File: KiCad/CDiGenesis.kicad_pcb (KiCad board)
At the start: 2 copper layers, 32 x 28 mm, 7 parts, among them J1 Genesis, J2 CDi, J3 Conn_01x03, U1 ATtiny1616-M

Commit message: Add silkscreen, nearing code completion
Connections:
- net /BTN_A/B renamed /BTN_B/A
- net /BTN_S/C renamed /BTN_C/S
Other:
- board text added: "+5V"
- board text added: "GND"
- board text added: "RTS"
- board text added: "RXD"
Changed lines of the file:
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@@
 	(net 2 "+5V")
 	(net 3 "/D_Up")
-	(net 4 "/BTN_A{slash}B")
-	(net 5 "/BTN_S{slash}C")
+	(net 4 "/BTN_B{slash}A")
+	(net 5 "/BTN_C{slash}S")
 	(net 6 "/D_Left")
 	(net 7 "/Select")
@@
 			(size 0.143431 0.143431)
 			(layers "F.Cu" "F.Mask" "F.Paste")
-			(net 4 "/BTN_A{slash}B")
+			(net 4 "/BTN_B{slash}A")
 			(pinfunction "PA2")
 			(pintype "bidirectional")
@@
 			(layers "F.Cu" "F.Mask" "F.Paste")
 			(roundrect_rratio 0.25)
-			(net 5 "/BTN_S{slash}C")
+			(net 5 "/BTN_C{slash}S")
 			(pinfunction "PA7")
 			(pintype "bidirectional")
@@
 			(layers "*.Cu" "*.Mask")
 			(remove_unused_layers no)
-			(net 4 "/BTN_A{slash}B")
+			(net 4 "/BTN_B{slash}A")
 			(pinfunction "6")
 			(pintype "passive")
@@
 			(layers "*.Cu" "*.Mask")
 			(remove_unused_layers no)
-			(net 5 "/BTN_S{slash}C")
+			(net 5 "/BTN_C{slash}S")
 			(pinfunction "9")
 			(pintype "passive")
@@
 		(layer "Edge.Cuts")
 	)
+	(gr_text "+5V"
+		(at 159.25 117.75 90)
+		(layer "F.SilkS")
+		(effects
+			(font
+				(size 0.5 0.5)
+				(thickness 0.1)
+				(bold yes)
+			)
+		)
+	)
 	(gr_text "+"
 		(at 148 124.25 90)
@@
 		)
 	)
+	(gr_text "RTS"
+		(at 154.900707 119.5 90)
+		(layer "F.SilkS")
+		(effects
+			(font
+				(size 0.5 0.5)
+				(thickness 0.1)
+				(bold yes)
+			)
+		)
+	)
+	(gr_text "GND"
+		(at 159.25 115.25 90)
+		(layer "F.SilkS")
+		(effects
+			(font
+				(size 0.5 0.5)
+				(thickness 0.1)
+				(bold yes)
+			)
+		)
+	)
 	(gr_text "p"
 		(at 148 123 90)
@@
 				(size 0.75 0.75)
 				(thickness 0.09375)
+			)
+		)
+	)
+	(gr_text "RXD"
+		(at 155.25 113.75 0)
+		(layer "F.SilkS")
+		(effects
+			(font
+				(size 0.5 0.5)
+				(thickness 0.1)
+				(bold yes)
 			)
 		)
@@
 	)
 	(zone
-		(net 5)
-		(net_name "/BTN_S{slash}C")
+		(net 15)
+		(net_name "/RTS")
 		(layer "F.Cu")
 		(name "$teardrop_padvia$")
 		(hatch none 0.1)
-		(priority 30004)
+		(priority 30002)
 		(attr
 			(teardrop
@@
 		(polygon
 			(pts
-				(xy 158.255 128.560041) (xy 158.055 128.560041) (xy 157.489824 129.700213) (xy 158.155 130.145669)
-				(xy 158.820176 129.700213)
+				(xy 153.673773 118.734806) (xy 153.815194 118.876227) (xy 155.06095 118.459148) (xy 154.900707 117.649293)
+				(xy 154.090852 117.48905)
 			)
 		)
 	)
 	(zone
-		(net 15)
-		(net_name "/RTS")
+		(net 9)
+		(net_name "/D_Right")
 		(layer "F.Cu")
 		(name "$teardrop_padvia$")
 		(hatch none 0.1)
-		(priority 30002)
+		(priority 30004)
 		(attr
 			(teardrop
@@
 		(polygon
 			(pts
-				(xy 153.673773 118.734806) (xy 153.815194 118.876227) (xy 155.06095 118.459148) (xy 154.900707 117.649293)
-				(xy 154.090852 117.48905)
+				(xy 156.87 125.720041) (xy 156.67 125.720041) (xy 156.104824 126.860213) (xy 156.77 127.305669)
+				(xy 157.435176 126.860213)
 			)
 		)
@@
 	)
 	(zone
-		(net 6)
-		(net_name "/D_Left")
+		(net 4)
+		(net_name "/BTN_B{slash}A")
 		(layer "F.Cu")
 		(name "$teardrop_padvia$")
 		(hatch none 0.1)
-		(priority 30007)
+		(priority 30002)
 		(attr
 			(teardrop
@@
 		(polygon
 			(pts
-				(xy 155.101 126.134668) (xy 154.901 126.134668) (xy 153.843928 126.520041) (xy 154 127.305669) (xy 154.784628 127.460741)
+				(xy 149.945 128.560041) (xy 149.745 128.560041) (xy 149.179824 129.700213) (xy 149.845 130.145669)
+				(xy 150.510176 129.700213)
 			)
 		)
@@
 	)
 	(zone
-		(net 7)
-		(net_name "/Select")
+		(net 5)
+		(net_name "/BTN_C{slash}S")
 		(layer "F.Cu")
 		(name "$teardrop_padvia$")
 		(hatch none 0.1)
-		(priority 30008)
+		(priority 30003)
 		(attr
 			(teardrop
@@
 		(polygon
 			(pts
-				(xy 154.036024 129.578157) (xy 153.894602 129.436735) (xy 152.771072 129.360041) (xy 152.614293 130.145376)
-				(xy 153.280176 130.589125)
+				(xy 158.255 128.560041) (xy 158.055 128.560041) (xy 157.489824 129.700213) (xy 158.155 130.145669)
+				(xy 158.820176 129.700213)
 			)
 		)
 	)
 	(zone
-		(net 4)
-		(net_name "/BTN_A{slash}B")
+		(net 6)
+		(net_name "/D_Left")
 		(layer "F.Cu")
 		(name "$teardrop_padvia$")
 		(hatch none 0.1)
-		(priority 30003)
+		(priority 30005)
 		(attr
 			(teardrop
@@
 		(polygon
 			(pts
-				(xy 149.945 128.560041) (xy 149.745 128.560041) (xy 149.179824 129.700213) (xy 149.845 130.145669)
-				(xy 150.510176 129.700213)
+				(xy 155.101 126.134668) (xy 154.901 126.134668) (xy 153.843928 126.520041) (xy 154 127.305669) (xy 154.784628 127.460741)
 			)
 		)
 	)
 	(zone
-		(net 9)
-		(net_name "/D_Right")
+		(net 2)
+		(net_name "+5V")
 		(layer "F.Cu")
 		(name "$teardrop_padvia$")
 		(hatch none 0.1)
-		(priority 30005)
+		(priority 30010)
 		(attr
 			(teardrop
@@
 		(polygon
 			(pts
-				(xy 156.87 125.720041) (xy 156.67 125.720041) (xy 156.104824 126.860213) (xy 156.77 127.305669)
-				(xy 157.435176 126.860213)
+				(xy 154.5 124.655764) (xy 154.3 124.655764) (xy 154.105764 125.191473) (xy 154.4 125.251) (xy 154.694236 125.191473)
 			)
 		)
 	)
 	(zone
-		(net 2)
-		(net_name "+5V")
+		(net 7)
+		(net_name "/Select")
 		(layer "F.Cu")
 		(name "$teardrop_padvia$")
 		(hatch none 0.1)
-		(priority 30010)
+		(priority 30006)
 		(attr
 			(teardrop
@@
 		(polygon
 			(pts
-				(xy 154.5 124.655764) (xy 154.3 124.655764) (xy 154.105764 125.191473) (xy 154.4 125.251) (xy 154.694236 125.191473)
-			)
-		)
+				(xy 154.036024 129.578157) (xy 153.894602 129.436735) (xy 152.771072 129.360041) (xy 152.614293 130.145376)
+				(xy 153.280176 130.589125)
+			)
+		)

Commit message: Effectively finalise code, remove SELECT nonsense
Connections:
- net /BTN_B/A renamed /BTN_B
- J1 pad 5: +5V -> unconnected-(J1-Pad5)
- J1 pad 7: /Select -> unconnected-(J1-Pad7)
- J1 pad 9: /BTN_C/S -> /BTN_C
- U1 pad 6: /Select -> /D_Right
- U1 pad 7: /D_Right -> /BTN_C
- U1 pad 8: /BTN_C/S -> unconnected-(U1-PA7-Pad8)
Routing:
- net /BTN_C/S: track 9.38 -> 0.00 mm
- net /BTN_C: track 0.00 -> 8.63 mm
- net /Select: track 8.44 -> 0.00 mm
- net /D_Right: track 5.22 -> 4.55 mm

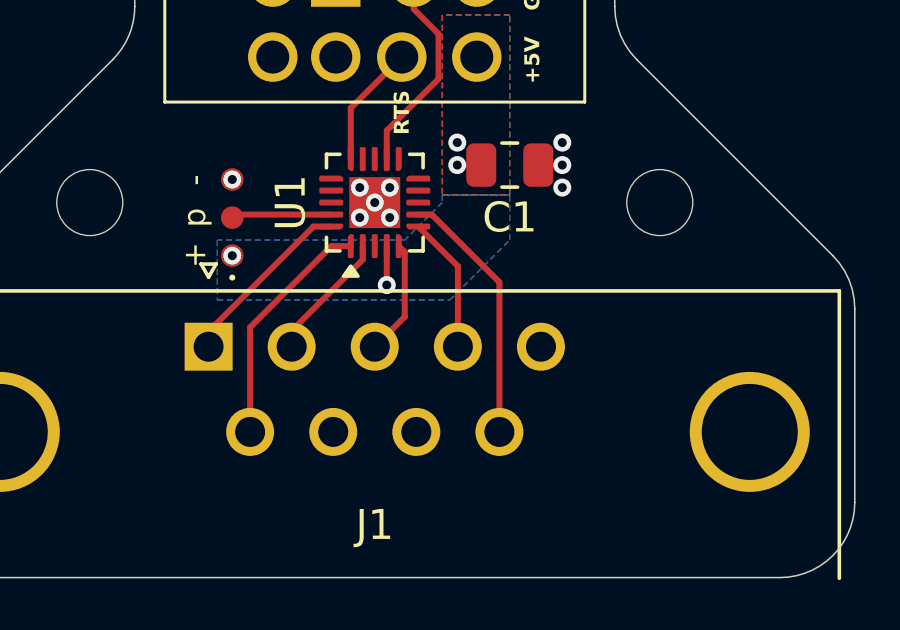
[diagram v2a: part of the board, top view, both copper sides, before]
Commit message: Revert PCB changes, will modify code
This reverts commit 0f8f6d9ed579b1546b77e135067905f4b0f0e6bf.
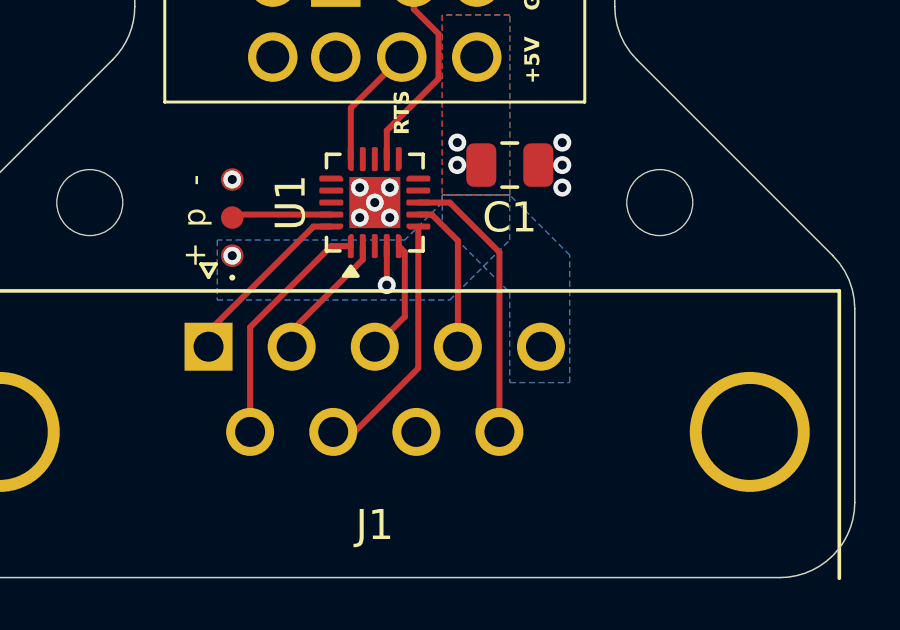
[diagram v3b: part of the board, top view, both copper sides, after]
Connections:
- net /BTN_B renamed /BTN_B/A
- J1 pad 5: unconnected-(J1-Pad5) -> +5V
- J1 pad 7: unconnected-(J1-Pad7) -> /Select
- J1 pad 9: /BTN_C -> /BTN_C/S
- U1 pad 6: /D_Right -> /Select
- U1 pad 7: /BTN_C -> /D_Right
- U1 pad 8: unconnected-(U1-PA7-Pad8) -> /BTN_C/S
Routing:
- net /BTN_C/S: track 0.00 -> 9.38 mm
- net /BTN_C: track 8.63 -> 0.00 mm
- net /Select: track 0.00 -> 8.44 mm
- net /D_Right: track 4.55 -> 5.22 mm
